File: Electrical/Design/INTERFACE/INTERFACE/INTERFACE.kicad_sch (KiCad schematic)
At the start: 55 parts, among them U5 BL1551B, U7 BL1551B, U8 BL1551B

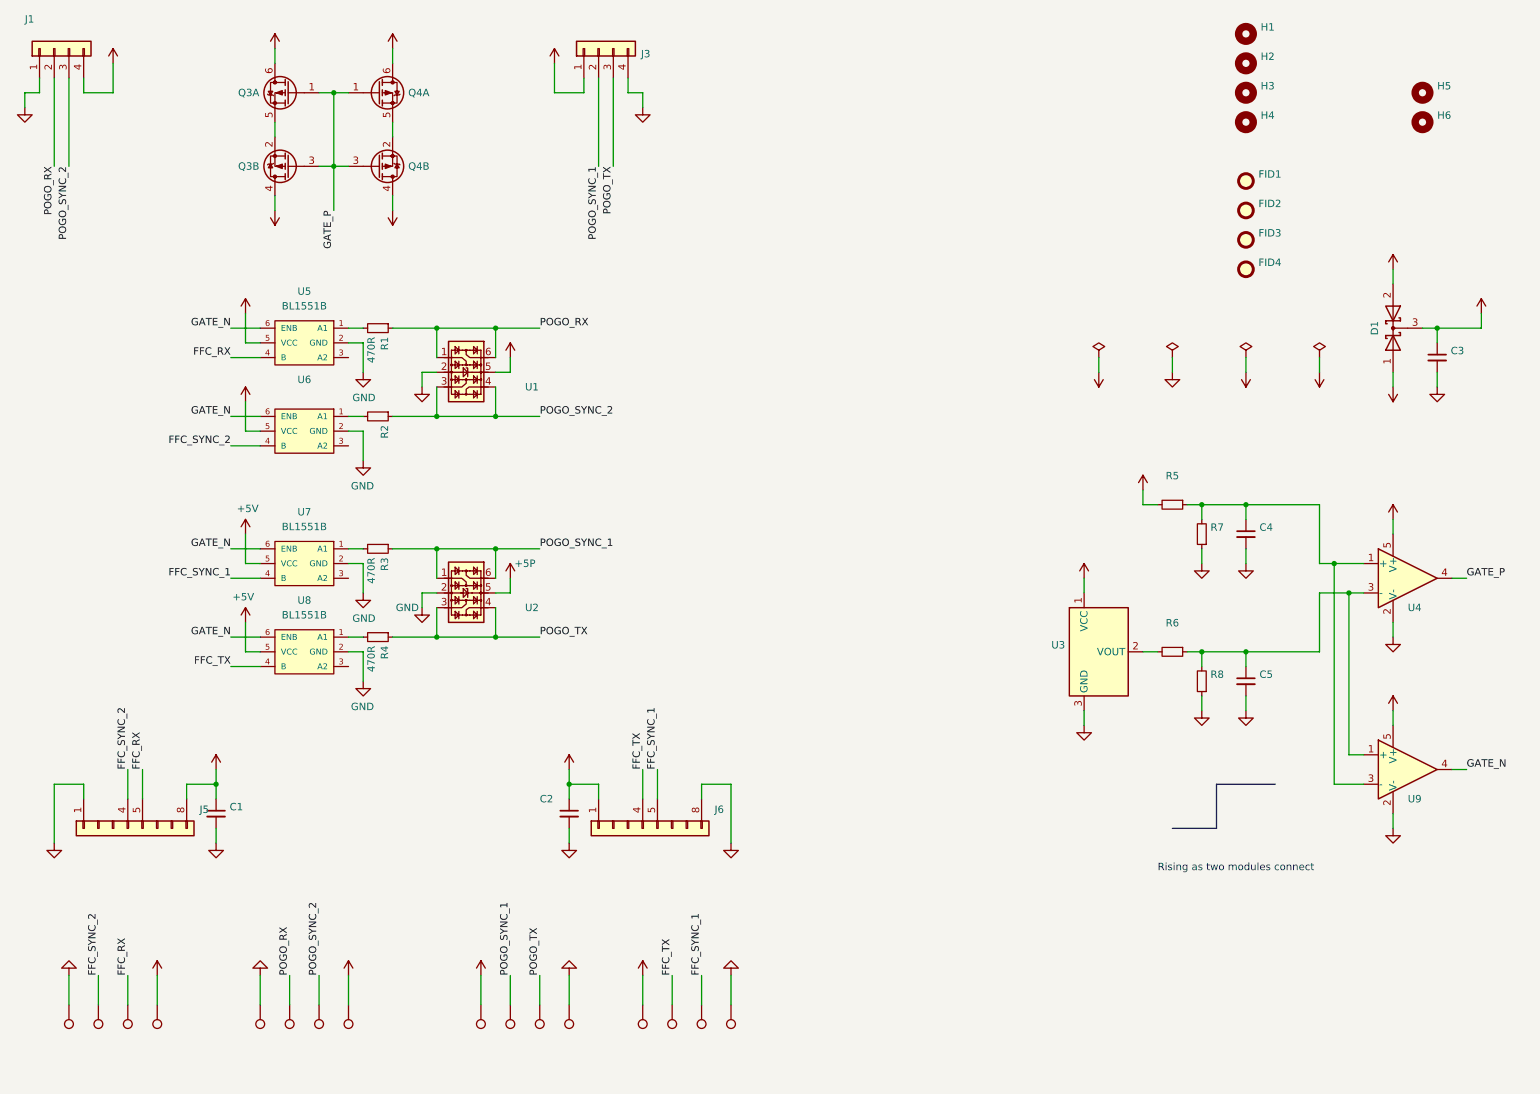
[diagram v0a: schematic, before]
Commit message: SUKU INTERFACE unconnected pins ERC fixed
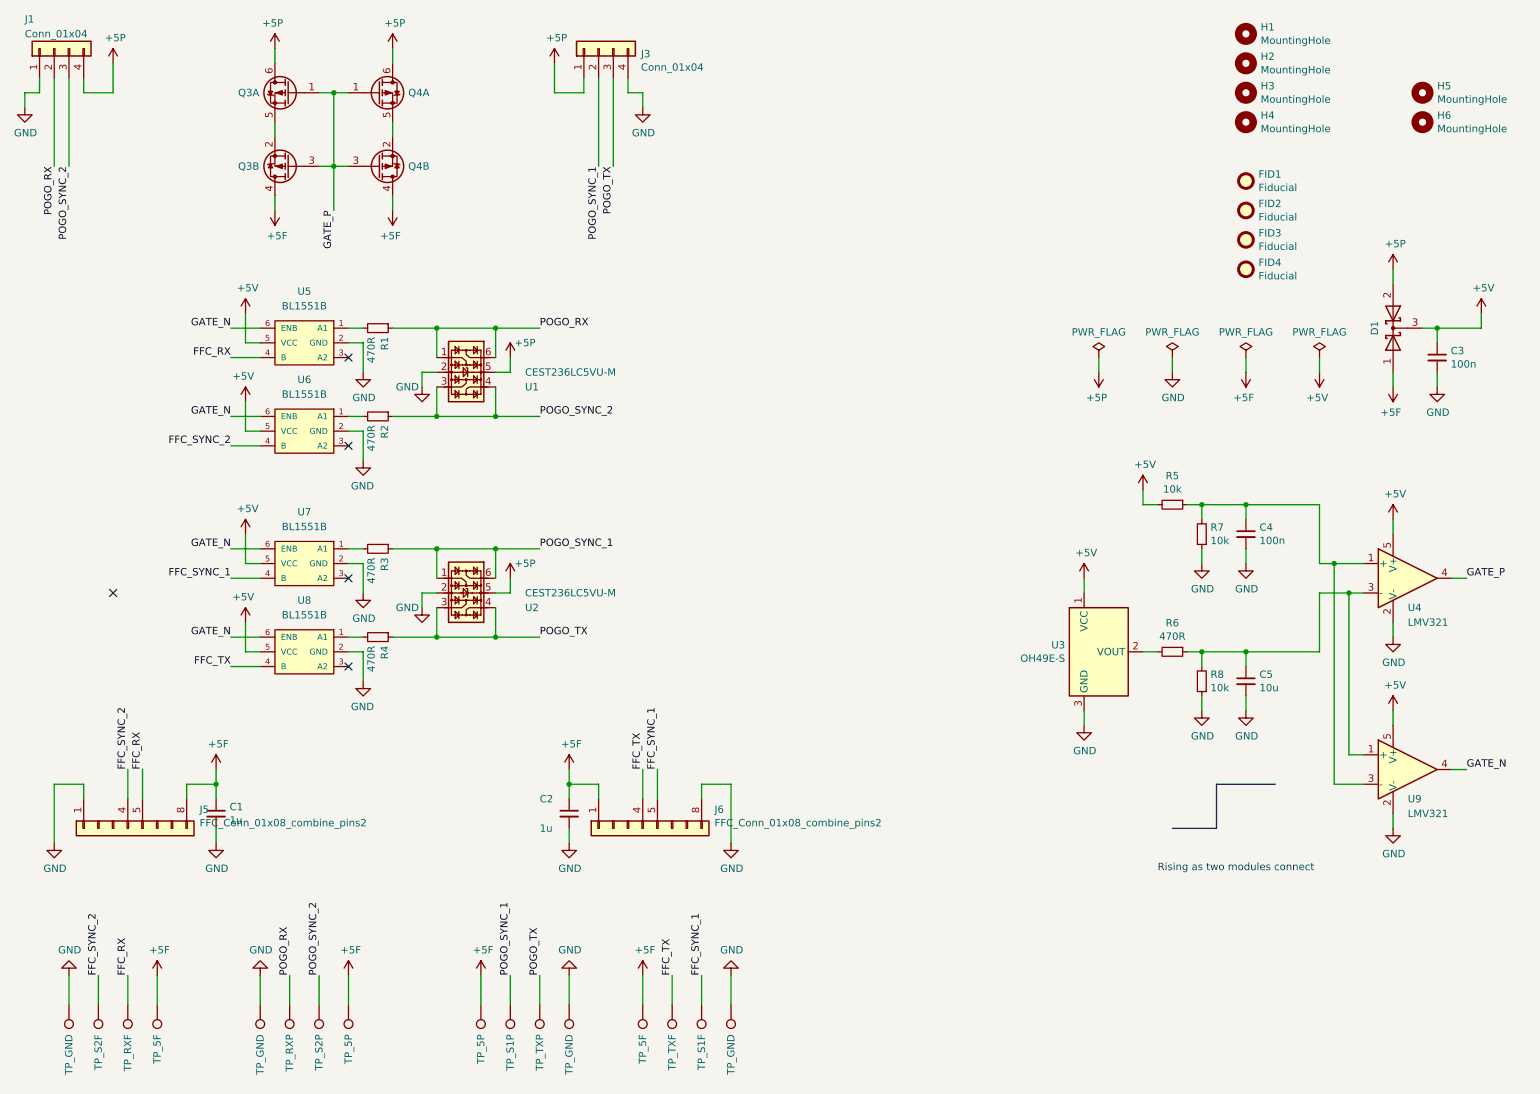
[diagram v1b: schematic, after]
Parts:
- C1, C2: value (none) -> 1u; footprint (none) -> suku_basics:CAP_0805
- C3, C4: value (none) -> 100n; footprint (none) -> suku_basics:CAP_0805
- C5: value (none) -> 10u; footprint (none) -> suku_basics:CAP_0805
- D1: value (none) -> BAT54C; footprint (none) -> suku_basics:SOT-23
- FID1, FID2, FID3, FID4: value (none) -> Fiducial; footprint (none) -> Fiducial:Fiducial_1.5mm_Mask3mm
- H1, H2, H3, H4: value (none) -> MountingHole; footprint (none) -> MountingHole:MountingHole_2.2mm_M2
- H5, H6: value (none) -> MountingHole; footprint (none) -> suku_basics:PANEL_BREAKOUT-2x3-0.7
- J1, J3: value (none) -> Conn_01x04; footprint (none) -> suku_basics:J_4xPOGO
- J5, J6: value (none) -> FFC_Conn_01x08_combine_pins2; footprint (none) -> suku_basics:J_FFC_1x8_Solder_3common
- Q3, Q4: value (none) -> WST2011; footprint (none) -> suku_basics:SOT-23-6
- R2, R6: value (none) -> 470R; footprint (none) -> suku_basics:RES_0805
- R5, R7, R8: value (none) -> 10k; footprint (none) -> suku_basics:RES_0805
- TP1, TP16, TP8, TP9: value (none) -> TP_GND; footprint (none) -> TestPoint:TestPoint_THTPad_1.0x1.0mm_Drill0.5mm
- TP10: value (none) -> TP_RXP; footprint (none) -> TestPoint:TestPoint_THTPad_1.0x1.0mm_Drill0.5mm
- TP11: value (none) -> TP_S2P; footprint (none) -> TestPoint:TestPoint_THTPad_1.0x1.0mm_Drill0.5mm
- TP12, TP13: value (none) -> TP_5P; footprint (none) -> TestPoint:TestPoint_THTPad_1.0x1.0mm_Drill0.5mm
- TP14: value (none) -> TP_S1P; footprint (none) -> TestPoint:TestPoint_THTPad_1.0x1.0mm_Drill0.5mm
- TP15: value (none) -> TP_TXP; footprint (none) -> TestPoint:TestPoint_THTPad_1.0x1.0mm_Drill0.5mm
- TP2: value (none) -> TP_S2F; footprint (none) -> TestPoint:TestPoint_THTPad_1.0x1.0mm_Drill0.5mm
- TP3: value (none) -> TP_RXF; footprint (none) -> TestPoint:TestPoint_THTPad_1.0x1.0mm_Drill0.5mm
- TP4, TP5: value (none) -> TP_5F; footprint (none) -> TestPoint:TestPoint_THTPad_1.0x1.0mm_Drill0.5mm
- TP6: value (none) -> TP_TXF; footprint (none) -> TestPoint:TestPoint_THTPad_1.0x1.0mm_Drill0.5mm
- TP7: value (none) -> TP_S1F; footprint (none) -> TestPoint:TestPoint_THTPad_1.0x1.0mm_Drill0.5mm
- U1, U2: value (none) -> CEST236LC5VU-M; footprint (none) -> suku_basics:SOT-23-6
- U3: value (none) -> OH49E-S; footprint (none) -> suku_basics:SOT-23W
- U4, U9: value (none) -> LMV321; footprint (none) -> suku_basics:SOT-23-5
- U5: footprint (none) -> suku_basics:SOT-363_SC-70-6
- U6: value (none) -> BL1551B; footprint (none) -> suku_basics:SOT-363_SC-70-6
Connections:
- no-connect marks 0 -> 5

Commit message: SUKU interface design updated for battery_conn
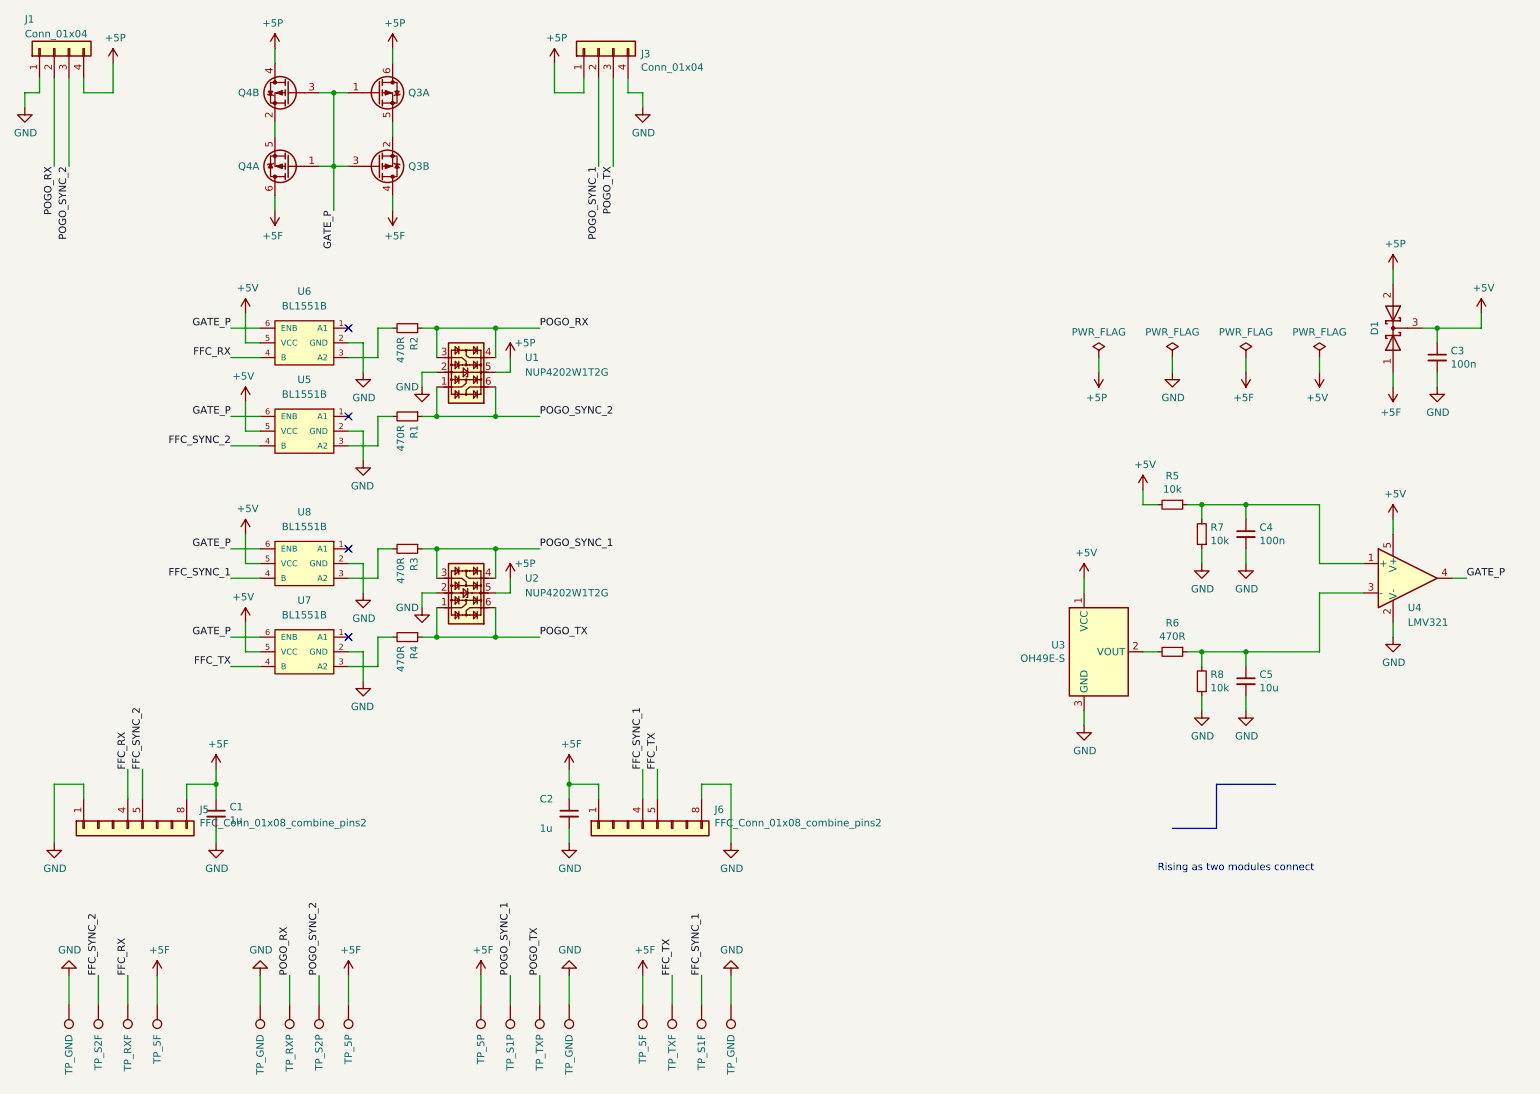
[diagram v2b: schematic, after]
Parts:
- removed FID1, FID2, FID3, FID4: Fiducial, Fiducial:Fiducial_1.5mm_Mask3mm, symbol Mechanical:Fiducial
- removed H1, H2, H3, H4: MountingHole, MountingHole:MountingHole_2.2mm_M2, symbol Mechanical:MountingHole
- removed H5, H6: MountingHole, suku_basics:PANEL_BREAKOUT-2x3-0.7, symbol Mechanical:MountingHole
- removed U9: LMV321, suku_basics:SOT-23-5, symbol Amplifier_Operational:LM321
- J1, J3: footprint suku_basics:J_4xPOGO -> suku_basics:J_4xPOGO_SMD
- J5, J6: footprint suku_basics:J_FFC_1x8_Solder_3common -> suku_basics:J_BATTERY_CONN
- R1, R2, R3, R4: footprint suku_basics:RES_0805 -> suku_basics:RES_0402
- U1, U2: value CEST236LC5VU-M -> NUP4202W1T2G; footprint suku_basics:SOT-23-6 -> suku_basics:SOT-363_SC-70-6
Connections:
- net GATE_N is gone; now on net GATE_P: U5.6 (ENB), U6.6 (ENB), U7.6 (ENB), U8.6 (ENB)
- net +5F: now also Q4.6 (D); no longer Q4.4 (D)
- net +5P: now also Q4.4 (D); no longer Q4.6 (D)
- net FFC_RX: now also J5.4 (Pin_4), U6.4 (B); no longer J5.5 (Pin_5), U5.4 (B)
- net FFC_SYNC_1: now also J6.4 (Pin_4), U8.4 (B); no longer J6.5 (Pin_5), U7.4 (B)
- net FFC_SYNC_2: now also J5.5 (Pin_5), U5.4 (B); no longer J5.4 (Pin_4), U6.4 (B)
- net FFC_TX: now also J6.5 (Pin_5), U7.4 (B); no longer J6.4 (Pin_4), U8.4 (B)
- net GATE_P: now also Q4.1 (G), Q4.3 (G); no longer Q4.1 (G), Q4.3 (G)
- net POGO_RX: now also R2.1, U1.3, U1.4; no longer R1.1, U1.1, U1.6
- net POGO_SYNC_1: now also U2.3, U2.4; no longer U2.1, U2.6
- net POGO_SYNC_2: now also R1.1, U1.1, U1.6; no longer R2.1, U1.3, U1.4
- net POGO_TX: now also U2.1, U2.6; no longer U2.3, U2.4
- net at R2.2: now also U6.3 (A2); no longer U6.1 (A1)
- net at U8.1 (A1): no longer R4.2
- net at U8.3 (A2): now also R3.2
- net at U7.1 (A1): no longer R3.2
- net at U7.3 (A2): now also R4.2
- net at U5.1 (A1): no longer R1.2
- net at U5.3 (A2): now also R1.2
- new net: Q4.2 (S), Q4.5 (S)
- no-connect marks 5 -> 4
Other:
- moved on the sheet: Q3A, Q3B, Q4A, Q4B, R1, R2, R3, R4, U5, U6, U7, U8

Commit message: SUKU footprint rescue reverted to default library parts
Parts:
- D1: symbol INTERFACE-rescue:D_Schottky_x2_KCom_AAK-Device -> Device:D_Schottky_Dual_CommonCathode_AAK
- Q3, Q4: symbol INTERFACE-rescue:Q_DUAL_PMOS_G1S2G2D2S1D1-Device -> Device:Q_Dual_PMOS_G1S2G2D2S1D1
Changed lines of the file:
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@@
     )
   )
-  (symbol (lib_id "INTERFACE-rescue:Q_DUAL_PMOS_G1S2G2D2S1D1-Device") (at 86.36 27.94 0) (unit 1)
+  (symbol (lib_id "Device:Q_Dual_PMOS_G1S2G2D2S1D1") (at 86.36 27.94 0) (unit 1)
     (in_bom yes) (on_board yes) (dnp no)
     (property "Reference" "Q3" (at 91.5924 27.94 0)
@@
     )
   )
-  (symbol (lib_id "INTERFACE-rescue:Q_DUAL_PMOS_G1S2G2D2S1D1-Device") (at 86.36 40.64 0) (mirror x) (unit 2)
+  (symbol (lib_id "Device:Q_Dual_PMOS_G1S2G2D2S1D1") (at 86.36 40.64 0) (mirror x) (unit 2)
     (in_bom yes) (on_board yes) (dnp no)
     (property "Reference" "Q3" (at 91.5924 40.64 0)
@@
     )
   )
-  (symbol (lib_id "INTERFACE-rescue:Q_DUAL_PMOS_G1S2G2D2S1D1-Device") (at 71.12 27.94 0) (mirror y) (unit 2)
+  (symbol (lib_id "Device:Q_Dual_PMOS_G1S2G2D2S1D1") (at 71.12 27.94 0) (mirror y) (unit 2)
     (in_bom yes) (on_board yes) (dnp no)
     (property "Reference" "Q4" (at 65.8876 27.94 0)
@@
     )
   )
-  (symbol (lib_id "INTERFACE-rescue:Q_DUAL_PMOS_G1S2G2D2S1D1-Device") (at 71.12 40.64 180) (unit 1)
+  (symbol (lib_id "Device:Q_Dual_PMOS_G1S2G2D2S1D1") (at 71.12 40.64 180) (unit 1)
     (in_bom yes) (on_board yes) (dnp no)
     (property "Reference" "Q4" (at 65.8876 40.64 0)
@@
     )
   )
-  (symbol (lib_id "INTERFACE-rescue:D_Schottky_x2_KCom_AAK-Device") (at 261.62 68.58 90) (unit 1)
+  (symbol (lib_id "Device:D_Schottky_Dual_CommonCathode_AAK") (at 261.62 68.58 90) (unit 1)
     (in_bom yes) (on_board yes) (dnp no)
     (property "Reference" "D1" (at 258.445 68.58 0)

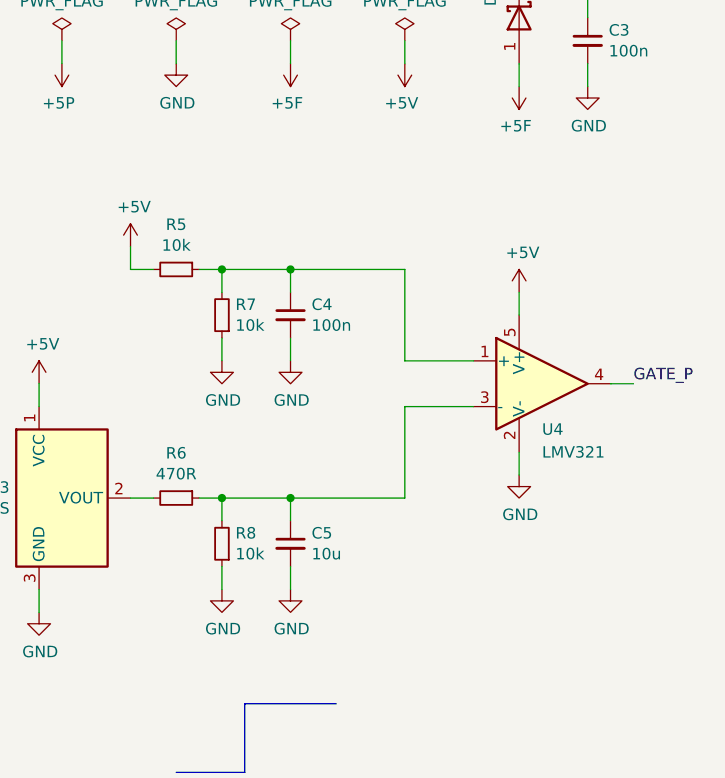
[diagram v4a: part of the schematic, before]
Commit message: SUKU interface testpoints added for comperator
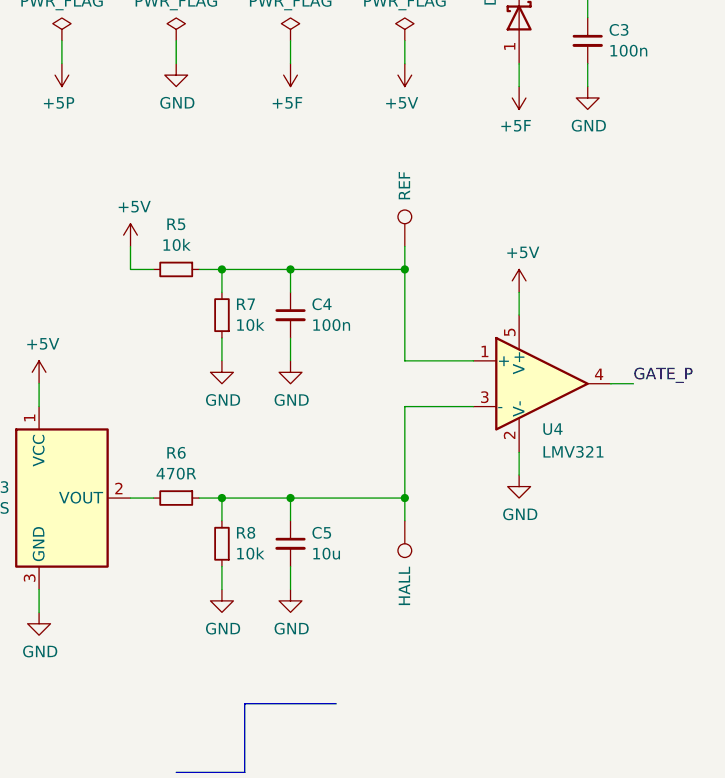
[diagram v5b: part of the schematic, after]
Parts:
- added TP17: REF, TestPoint:TestPoint_THTPad_1.0x1.0mm_Drill0.5mm, symbol Connector:TestPoint
- added TP18: HALL, TestPoint:TestPoint_THTPad_1.0x1.0mm_Drill0.5mm, symbol Connector:TestPoint
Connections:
- net at C5.1, R6.1, R8.2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: now also TP18.1
- net at C4.1, R5.1, R7.2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: now also TP17.1
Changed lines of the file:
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@@
   (junction (at 96.52 121.92) (diameter 0) (color 0 0 0 0)
   )
+  (junction (at 248.92 99.06) (diameter 0) (color 0 0 0 0)
+  )
   (junction (at 228.6 99.06) (diameter 0) (color 0 0 0 0)
   )
@@
   )
   (junction (at 269.24 68.58) (diameter 0) (color 0 0 0 0)
+  )
+  (junction (at 248.92 124.46) (diameter 0) (color 0 0 0 0)
   )
   (junction (at 96.52 83.82) (diameter 0) (color 0 0 0 0)
@@
     (stroke (width 0) (type default))
   )
+  (wire (pts (xy 248.92 96.52) (xy 248.92 99.06))
+    (stroke (width 0) (type default))
+  )
   (wire (pts (xy 137.16 180.34) (xy 137.16 185.42))
     (stroke (width 0) (type default))
@@
   )
   (wire (pts (xy 96.52 68.58) (xy 106.68 68.58))
+    (stroke (width 0) (type default))
+  )
+  (wire (pts (xy 248.92 124.46) (xy 248.92 127))
     (stroke (width 0) (type default))
   )
@@
     )
   )
+  (symbol (lib_id "Connector:TestPoint") (at 248.92 127 0) (mirror x) (unit 1)
+    (in_bom yes) (on_board yes) (dnp no)
+    (property "Reference" "TP18" (at 250.3932 129.9972 0)
+      (effects (font (size 1.27 1.27)) (justify left) hide)
+    )
+    (property "Value" "HALL" (at 248.92 132.08 90)
+      (effects (font (size 1.27 1.27)) (justify left))
+    )
+    (property "Footprint" "TestPoint:TestPoint_THTPad_1.0x1.0mm_Drill0.5mm" (at 254 127 0)
+      (effects (font (size 1.27 1.27)) hide)
+    )
+    (property "Datasheet" "~" (at 254 127 0)
+      (effects (font (size 1.27 1.27)) hide)
+    )
+    (pin "1")
+    (instances
+      (project "INTERFACE"
+        (path "/3a7648d8-121a-4921-9b92-9b35b76ce39b"
+          (reference "TP18") (unit 1)
+        )
+      )
+    )
+  )
   (symbol (lib_id "power:GND") (at 93.98 116.84 0) (unit 1)
     (in_bom yes) (on_board yes) (dnp no)
@@
         )
       )
+    )
+  )
+  (symbol (lib_id "Connector:TestPoint") (at 248.92 96.52 0) (mirror y) (unit 1)
+    (in_bom yes) (on_board yes) (dnp no)
+    (property "Reference" "TP17" (at 247.4468 93.5228 0)
+      (effects (font (size 1.27 1.27)) (justify left) hide)
+    )
+    (property "Value" "REF" (at 248.92 91.44 90)
+      (effects (font (size 1.27 1.27)) (justify left))
+    )
+    (property "Footprint" "TestPoint:TestPoint_THTPad_1.0x1.0mm_Drill0.5mm" (at 243.84 96.52 0)
+      (effects (font (size 1.27 1.27)) hide)
+    )
+    (property "Datasheet" "~" (at 243.84 96.52 0)
+      (effects (font (size 1.27 1.27)) hide)
+    )
+    (pin "1")
+    (instances
+      (project "INTERFACE"
+        (path "/3a7648d8-121a-4921-9b92-9b35b76ce39b"
+          (reference "TP17") (unit 1)
+        )
+      )
